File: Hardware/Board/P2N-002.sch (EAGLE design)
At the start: 38 parts, among them IC1 4053N, IC2 LTC485N, IC3 74LS07N, IC4 LTC485N, K1 G5V1, T1 2SC1815

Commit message: New layout.
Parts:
- added JP6: (no value), pinhead:PINHD-1X3
- JP2: device pinhead:PINHD-1X5/90 -> pinhead:PINHD-1X4
- JP3: device pinhead:PINHD-1X4 -> pinhead:PINHD-1X14
- JP4: device pinhead:PINHD-1X3 -> pinhead:PINHD-1X2
- JP5: device pinhead:PINHD-1X14 -> pinhead:PINHD-1X5/90
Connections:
- new net N$30: JP4.1, MC1.9
- new net N$31: JP4.2, MC1.10
- net ANLG0: now also JP3.8; no longer JP5.8
- net ANLG1: now also JP3.9; no longer JP5.9
- net ANLG2: now also JP3.10; no longer JP5.10
- net ANLG3: now also JP3.11; no longer JP5.11
- net GND: now also JP3.14, JP5.5, R3.2, R4.2; no longer JP2.5, JP3.4, JP5.14, JP5.2
- net MIDI14: no longer MC1.4
- net MIDIRX: now also JP6.1; no longer JP4.1
- net N$17: now also JP2.2; no longer JP3.1
- net N$18: now also JP2.4; no longer JP3.3
- net N$20: now also JP2.1; no longer R3.2
- net N$21: now also JP2.3; no longer R4.2
- net N$22: now also MC1.12; no longer MC1.8
- net N$24: now also JP3.5, JP5.1, MC1.8; no longer JP2.1, JP5.5, MC1.10
- net N$25: now also JP3.4, JP5.2; no longer JP2.2, JP5.4
- net N$26: now also JP3.3; no longer JP2.3
- net N$27: now also JP3.6, MC1.6; no longer JP5.6, MC1.9
- net N$28: now also JP3.12; no longer JP5.12
- net N$29: now also JP3.13; no longer JP5.13
- net N$7: now also JP6.2; no longer JP4.2
- net N$9: now also MC1.4; no longer MC1.6
- net VCC: now also JP3.7; no longer JP5.7
- net VDD: now also JP3.1; no longer JP5.1
- net XMIDIRX: now also JP6.3; no longer JP4.3
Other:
- moved on the sheet: R3, R4

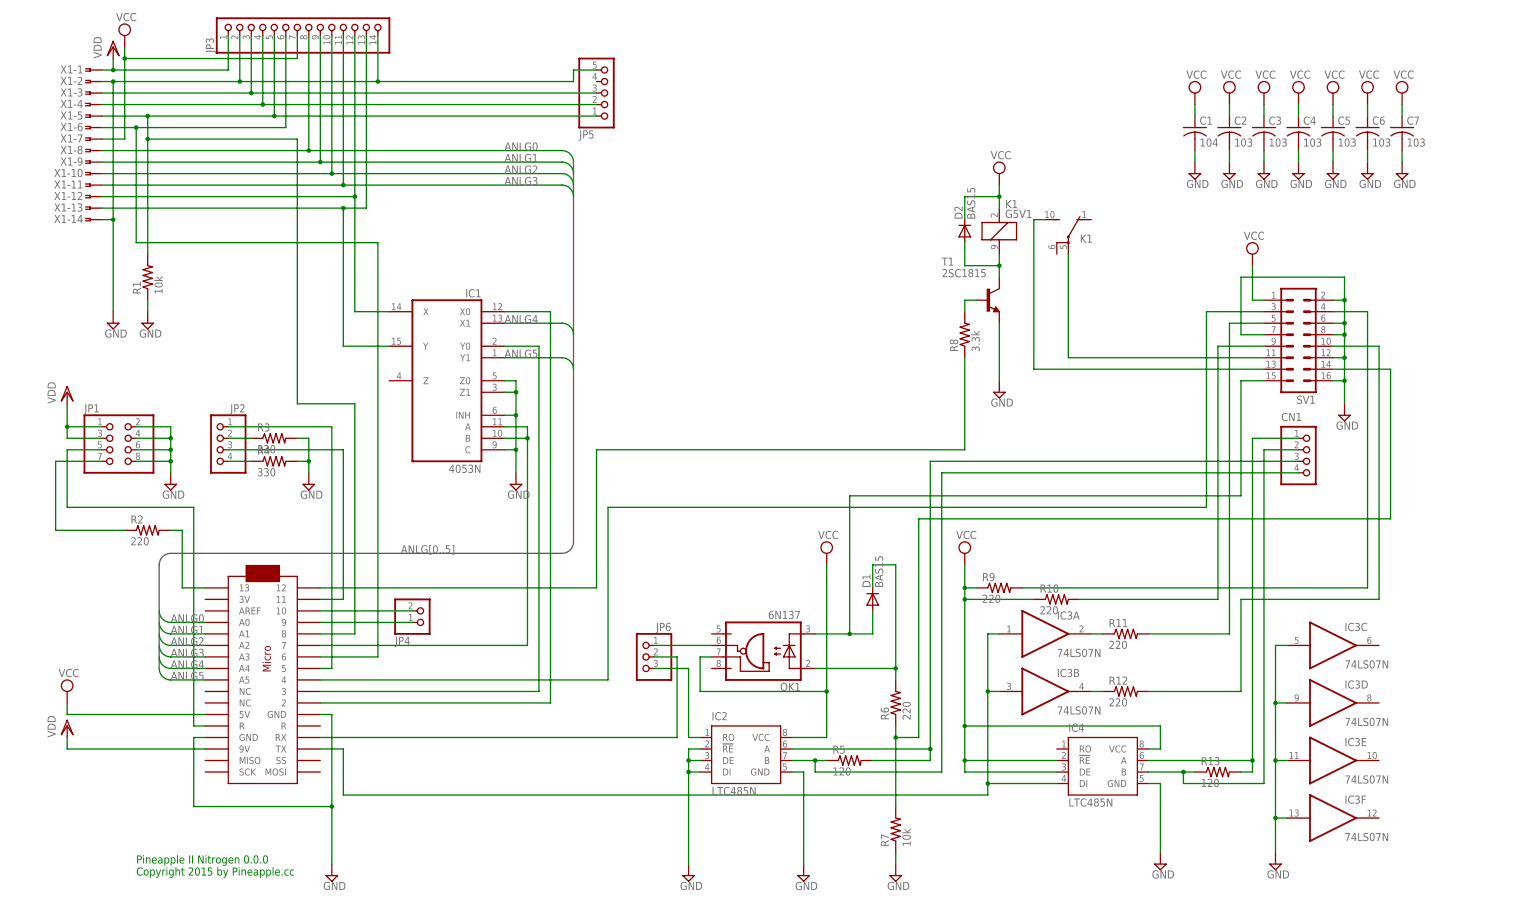
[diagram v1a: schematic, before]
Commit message: Changed MIDI IN/OUT layout.
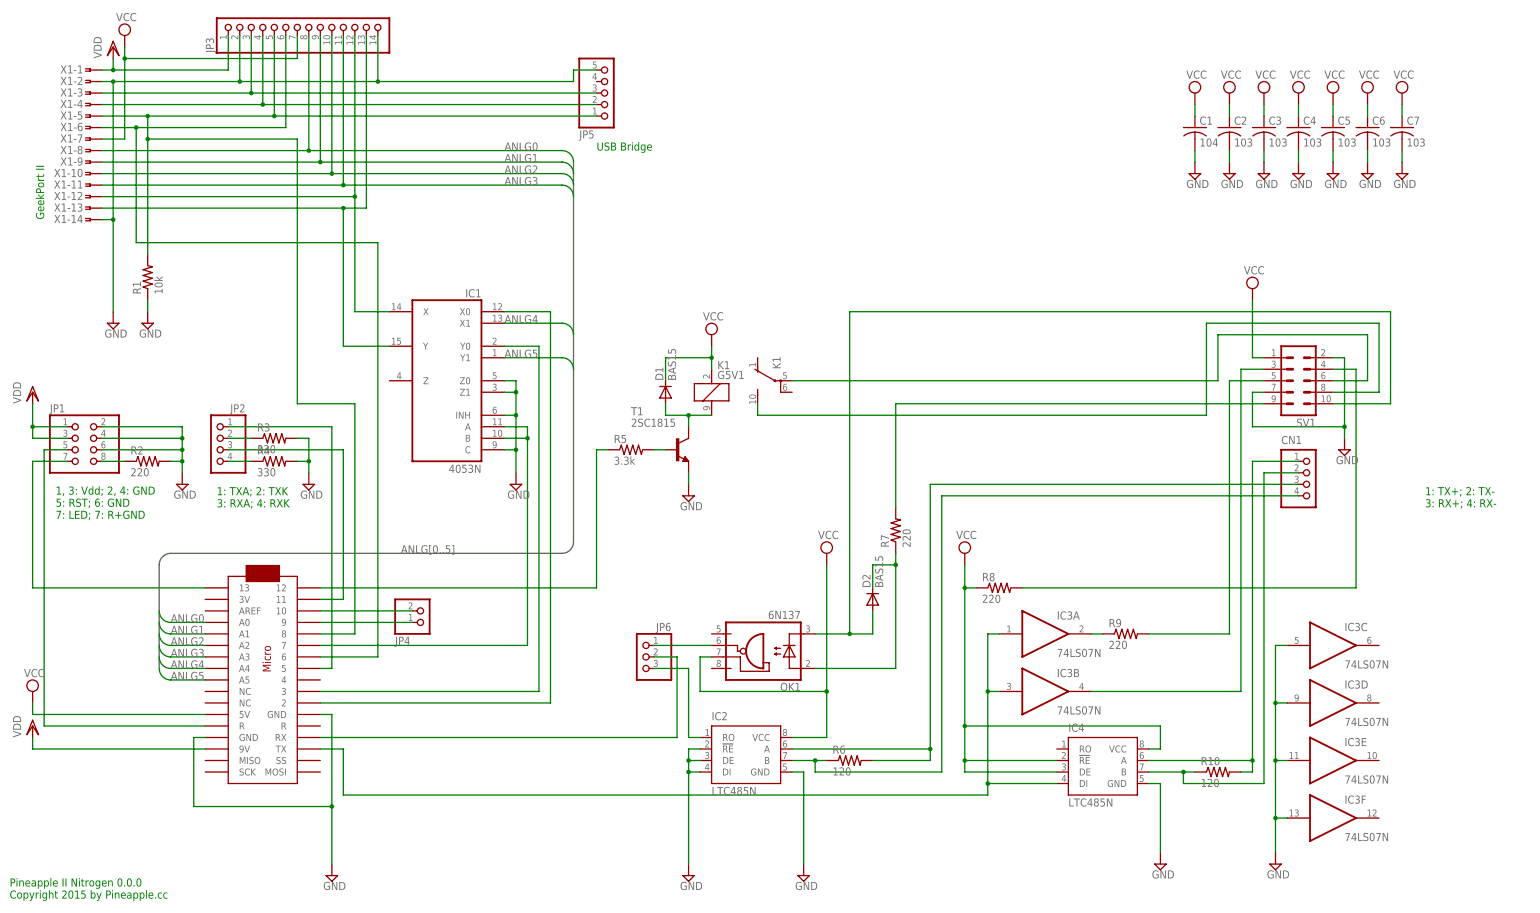
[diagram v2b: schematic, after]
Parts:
- removed R11, R12: 220, resistor:R-US_0204/5
- removed R13: 120, resistor:R-US_0204/5
- R10, R6: value 220 -> 120
- R5: value 120 -> 3.3k
- R7: value 10k -> 220
- R8: value 3.3k -> 220
- SV1: device con-ml:ML16L -> con-ml:ML10L
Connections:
- removed net MIDI14: R6.1, R7.2, SV1.14
- removed net N$11: R10.2, SV1.9
- removed net N$13: R12.2, SV1.10
- removed net N$9: MC1.4, SV1.3
- new net N$32: JP1.8, R2.1
- net GND: now also R2.2; no longer JP1.8, R7.1, SV1.12, SV1.16, SV1.6, SV1.8
- net MIDI1: now also R10.2; no longer R13.2
- net MIDI11: now also R6.2; no longer R5.2
- net MIDI13: now also R6.1; no longer R5.1
- net MIDI15: now also D2.A, SV1.10; no longer D1.A, SV1.15
- net MIDI3: now also R10.1; no longer R13.1
- net N$1: now also SV1.3; no longer R12.1
- net N$10: now also R9.2; no longer R11.2
- net N$12: now also R8.2; no longer R9.2
- net N$14: now also SV1.8; no longer SV1.13
- net N$15: now also D2.C, R7.1; no longer D1.C, R6.2
- net N$16: now also SV1.6; no longer SV1.11
- net N$2: now also R9.1; no longer R11.1
- net N$22: now also R5.1; no longer R8.1
- net N$4: now also MC1.13; no longer R2.1
- net N$5: now also R7.2, SV1.9; no longer MC1.13, R2.2
- net N$6: now also D1.A; no longer D2.A
- net N$8: now also R5.2; no longer R8.2
- net VCC: now also D1.C, R8.1; no longer D2.C, R10.1, R9.1
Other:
- note added: "1, 3: Vdd; 2, 4: GND 5: RST; 6: GND 7: LED; 7: R+GND"
- note added: "1: TX+; 2: TX- 3: RX+; 4: RX-"
- note added: "1: TXA; 2: TXK 3: RXA; 4: RXK"
- note added: "GeekPort II"
- note added: "USB Bridge"
- moved on the sheet: CN1, D1, D2, JP1, K1, R10, R2, R5, R6, R7, R8, R9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

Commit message: Internal drive port.
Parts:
- removed C6, C7: 103, rcl:C-US025-025X050
- removed JP6: (no value), pinhead:PINHD-1X3
- added S1: TL36PO, switch:TL36PO
- JP4: device pinhead:PINHD-1X2 -> pinhead:PINHD-2X3
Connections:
- new net N$11: JP4.5, MC1.MOSI
- new net N$13: JP4.6, MC1.SCK
- new net N$33: JP4.4, MC1.MISO
- new net N$9: JP4.3, MC1.4
- net GND: no longer C6.2, C7.2
- net MIDIRX: now also S1.O; no longer JP6.1
- net N$7: now also S1.P; no longer JP6.2
- net VCC: no longer C6.1, C7.1
- net XMIDIRX: now also S1.S; no longer JP6.3
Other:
- moved on the sheet: D1, K1, R5, T1
